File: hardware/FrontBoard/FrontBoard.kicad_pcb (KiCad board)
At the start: 2 copper layers, 45 x 80 mm, 33 parts, among them J3 from main board, J4 from main board, J8 panel jacks, SW1 EC11 SEL, SW2 EC11 A, SW3 EC11 B, SW4 RUN, SW5 BOOT

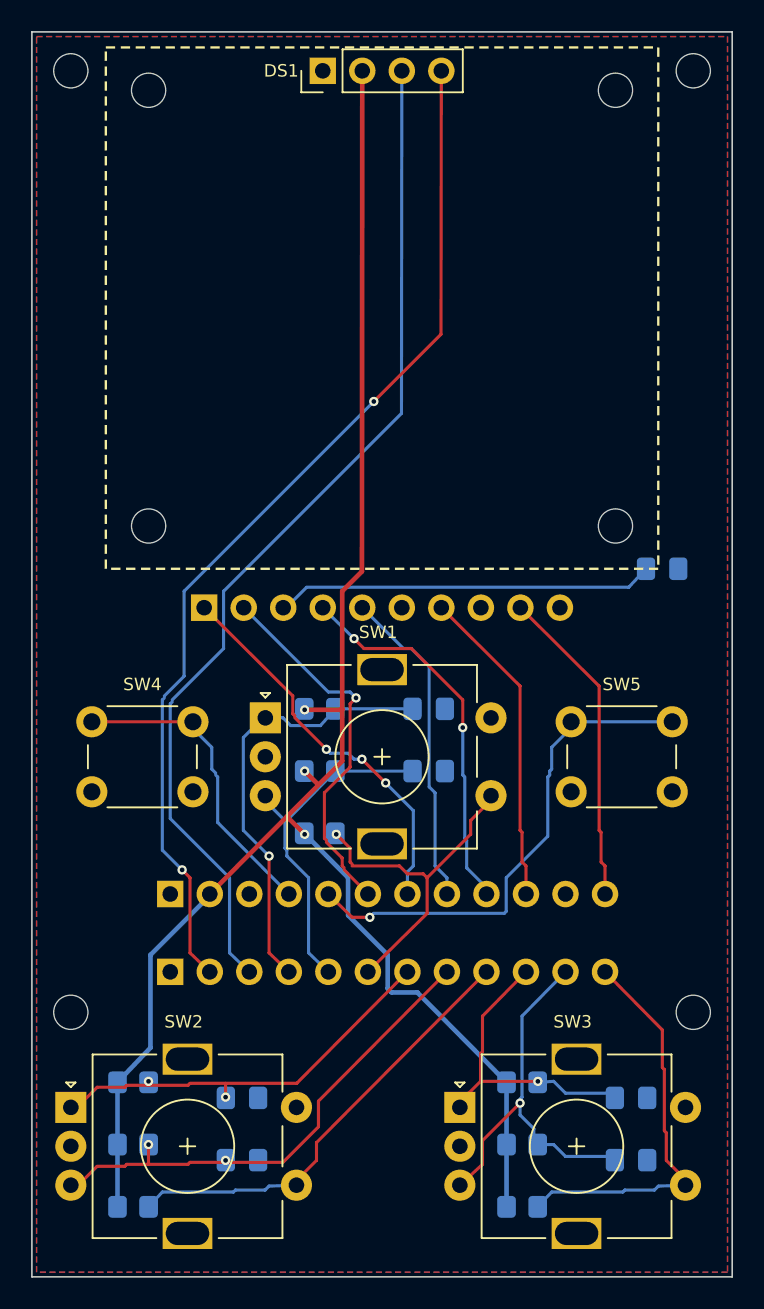
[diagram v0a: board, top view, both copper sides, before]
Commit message: The display's pin 1 is VDD, not GND
Measured on the part now in hand: 1 VDD, 2 GND, 3 SCK, 4 SDA, numbered from the
display side with pin 1 on the left. The symbol had the order most modules use
-- GND, VCC, SCL, SDA -- so the board as drawn would have put 3.3 V on the
module's ground pin and ground on its supply. The display would not have
survived first power-up. The README has been warning about exactly this since
the schematic was drawn ("some vendors swap the first two"); it turns out this
vendor is one of them.

The fix is two pins swapped in the symbol and the two power symbols exchanged in
the sheet, which changes the netlist, so the front board is re-routed: 230
segments, 19 vias, still no failures. The header position needed no change --
it is centred on the module and the module is centred on the board, so DS1 was
already where it belongs, with pin 1 on the left.

Also carried across while the boards were open: DNP and exclude-from-BOM now
travel from the symbols to the footprints, so schematic parity is clean rather
than clean-if-you-only-look-at-errors.

Still assumed, and now the only thing that is: the display's four mounting holes
at 30 x 28 mm. They are non-plated and carry nothing, so being wrong costs a
standoff rather than a board, but they have not been measured.

Co-Authored-By: Claude Fable 5 <noreply@anthropic.com>
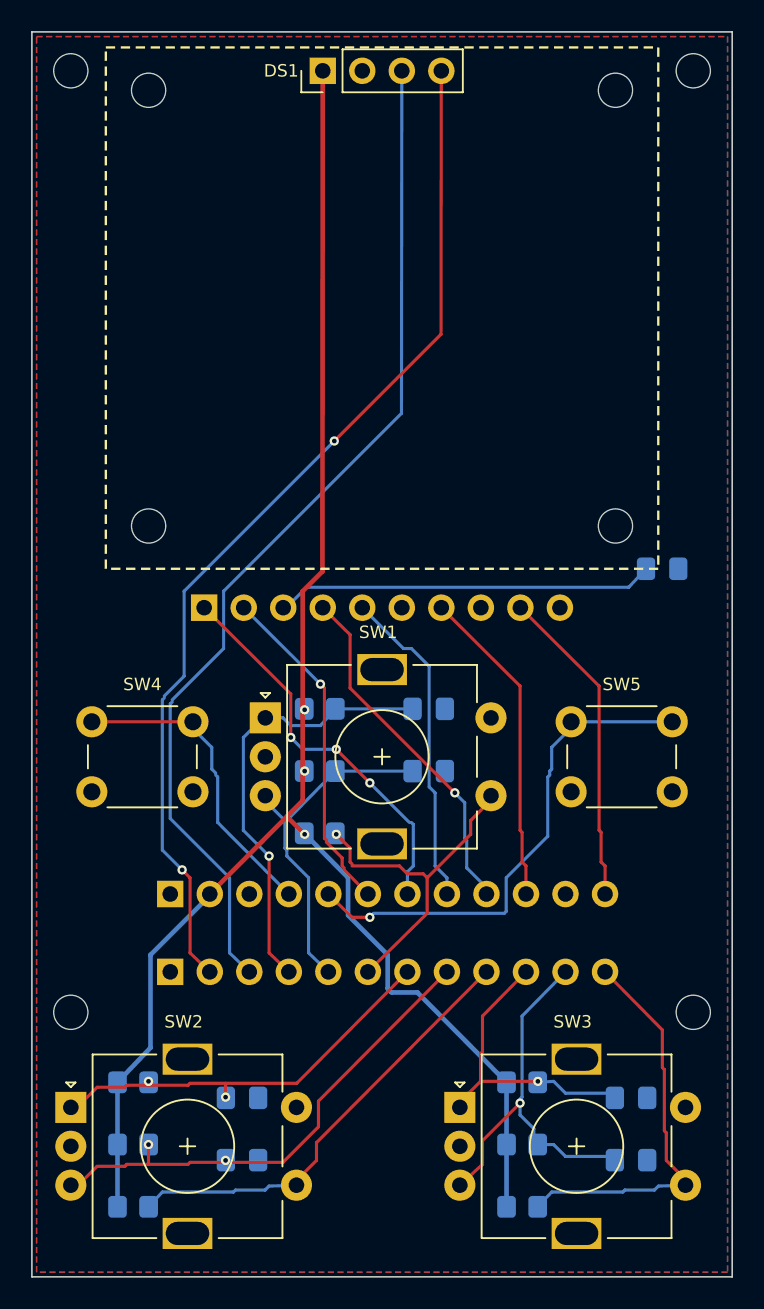
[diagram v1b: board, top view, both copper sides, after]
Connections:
- DS1 pad 1: GND -> +3V3
- DS1 pad 2: +3V3 -> GND
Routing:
- net +3V3: track 115.0 -> 110.3 mm
- net MIDI_IN_4: track 24.0 -> 21.4 mm
- net MIDI_OUT_5: track 24.5 -> 22.8 mm, vias 2 -> 1

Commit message: Measure the last thing that was still assumed
The display's four M2 holes: 30.4 x 28.5 mm apart, 2.5 mm in from the module's
top-left corner, off the part itself. The layout had them at 30 x 28 -- carried
over from the first draft of this document and never checked -- so they were
0.4 and 0.5 mm out. Small enough to look right and big enough that an M2 screw
would not go in.

The numbers also confirm the module: 2.5 + 30.4 + 2.5 is 35.4 and
2.5 + 28.5 + 2.5 is 33.5, exactly the outline this document has been carrying
since before anyone had the part.

Front board re-routed around the moved holes, 230 segments and 19 vias, no
failures, DRC clean. The drill file now carries the four holes at 30.40 x 28.50,
checked in the exported Excellon rather than in the board.

With this, nothing on either board rests on an assumption: every footprint
position comes from a datasheet, a STEP model, the panel drawing, or a
measurement on the part in hand.

Co-Authored-By: Claude Fable 5 <noreply@anthropic.com>
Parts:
- moved H2 0.32 mm to (37.7, 3.50)
- moved H4 0.32 mm to (37.7, 32.0)
- moved H1 0.32 mm to (7.30, 3.50)
- moved H3 0.32 mm to (7.30, 32.0)
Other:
- board text added: "OLED module 35.4 x 33.5, holes 30.4 x 28.5 measured on the part. DS1 is centred on the module top edge, pin 1 = VDD on the left."
- board text removed: "OLED module outline. DS1 is drawn on the module top edge -- verify the header position against the module before ordering."
